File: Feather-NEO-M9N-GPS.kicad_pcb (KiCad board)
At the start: 2 copper layers, 50.8 x 22.9 mm, 60 parts, among them IC1 PRTR5V0U2F,115, J6 USB_B_Micro, U1 NEO-M9N, U2 AP2112K-3.3

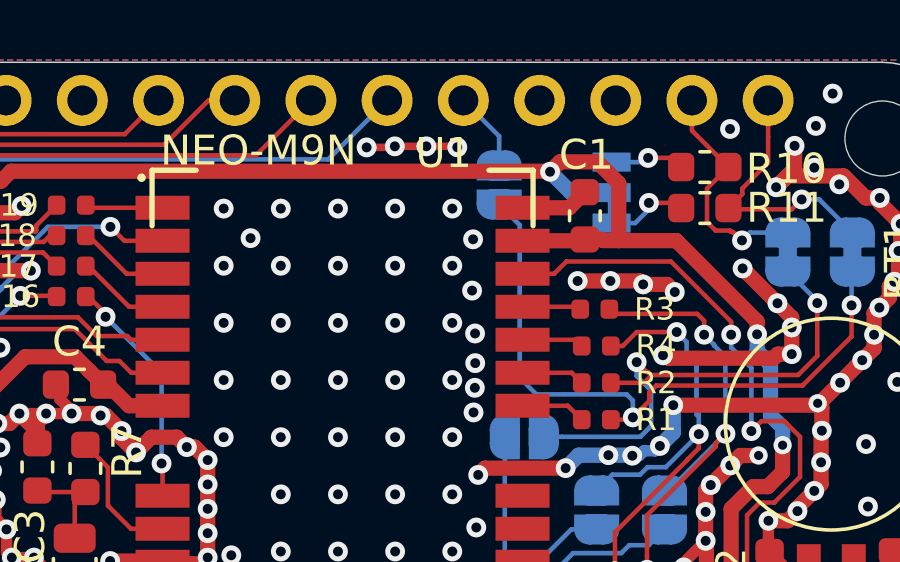
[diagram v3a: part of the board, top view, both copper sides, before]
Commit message: Added additional CS pin. Kept caps as is because of integration manual
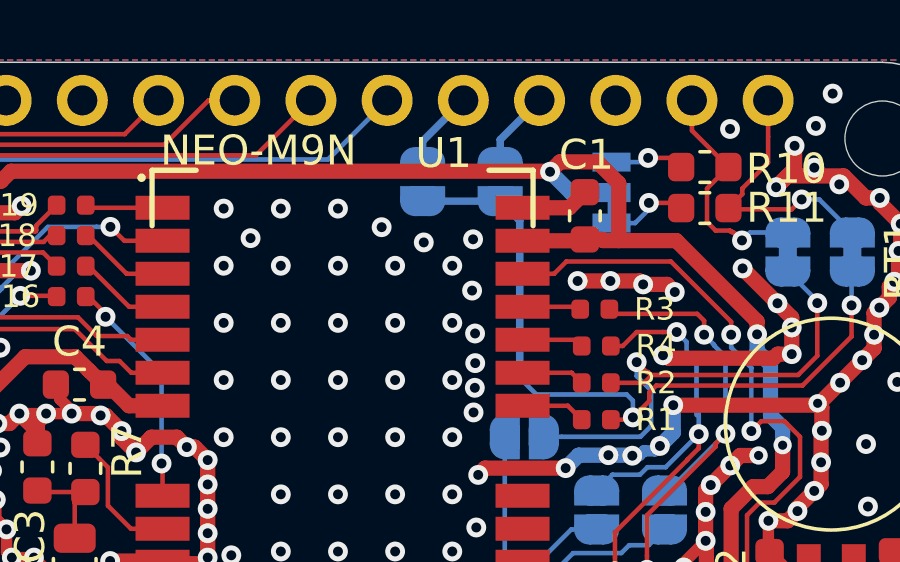
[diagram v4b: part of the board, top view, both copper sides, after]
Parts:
- added JP17: ~CS2, Jumper:SolderJumper-2_P1.3mm_Open_RoundedPad1.0x1.5mm, B.Cu at (164.2, 78.5)
- R13: value 1k -> 500
- moved JP16 2.55 mm to (161.6, 78.5)
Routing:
- net GND: track 237.1 -> 234.0 mm, vias 238 -> 234
- net Net-(JP16-Pad2): track 22.9 -> 25.5 mm
- net /6: track 0.00 -> 2.60 mm
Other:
- board text added: "6"
- board text added: "Rev2.4 ABW 3/6/20"
- board text removed: "Rev2.3 ABW 2/24/20"
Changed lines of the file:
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@@
   (general
     (thickness 1.6)
-    (drawings 21)
-    (tracks 1105)
+    (drawings 22)
+    (tracks 1099)
     (zones 0)
-    (modules 60)
+    (modules 61)
     (nets 73)
   )
@@
   )
   (setup
-    (last_trace_width 0.381)
+    (last_trace_width 0.1524)
     (user_trace_width 0.1524)
     (user_trace_width 0.1778)
@@
       (drillshape 0)
       (scaleselection 1)
-      (outputdirectory "Rev2.3/"))
+      (outputdirectory "Rev2.4/"))
   )
   (net 0 "")
@@
   )
   (module Jumper:SolderJumper-2_P1.3mm_Open_RoundedPad1.0x1.5mm (layer B.Cu)
+    (at 164.15766 78.47584 270)
+    (descr "SMD Solder Jumper, 1x1.5mm, rounded Pads, 0.3mm gap, open")
+    (tags "solder jumper open")
+    (attr virtual)
+    (fp_text reference JP17 (at 0 1.8 90) (layer B.Fab)
+      (effects (font (size 1 1) (thickness 0.15)) (justify mirror))
+    )
+    (fp_text value ~CS2 (at 0 -1.9 90) (layer B.Fab)
+      (effects (font (size 1 1) (thickness 0.15)) (justify mirror))
+    )
+    (fp_line (start 1.65 -1.25) (end -1.65 -1.25) (layer B.CrtYd) (width 0.05))
+    (fp_line (start 1.65 -1.25) (end 1.65 1.25) (layer B.CrtYd) (width 0.05))
+    (fp_line (start -1.65 1.25) (end -1.65 -1.25) (layer B.CrtYd) (width 0.05))
+    (fp_line (start -1.65 1.25) (end 1.65 1.25) (layer B.CrtYd) (width 0.05))
+    (fp_line (start -0.7 1) (end 0.7 1) (layer B.SilkS) (width 0.12))
+    (fp_line (start 1.4 0.3) (end 1.4 -0.3) (layer B.SilkS) (width 0.12))
+    (fp_line (start 0.7 -1) (end -0.7 -1) (layer B.SilkS) (width 0.12))
+    (fp_line (start -1.4 -0.3) (end -1.4 0.3) (layer B.SilkS) (width 0.12))
+    (fp_arc (start -0.7 0.3) (end -0.7 1) (angle 90) (layer B.SilkS) (width 0.12))
+    (fp_arc (start -0.7 -0.3) (end -1.4 -0.3) (angle 90) (layer B.SilkS) (width 0.12))
+    (fp_arc (start 0.7 -0.3) (end 0.7 -1) (angle 90) (layer B.SilkS) (width 0.12))
+    (fp_arc (start 0.7 0.3) (end 1.4 0.3) (angle 90) (layer B.SilkS) (width 0.12))
+    (pad 2 smd custom (at 0.65 0 270) (size 1 0.5) (layers B.Cu B.Mask)
+      (net 72 "Net-(JP16-Pad2)") (zone_connect 2)
+      (options (clearance outline) (anchor rect))
+      (primitives
+        (gr_circle (center 0 -0.25) (end 0.5 -0.25) (width 0))
+        (gr_circle (center 0 0.25) (end 0.5 0.25) (width 0))
+        (gr_poly (pts
+           (xy 0 0.75) (xy -0.5 0.75) (xy -0.5 -0.75) (xy 0 -0.75)) (width 0))
+      ))
+    (pad 1 smd custom (at -0.65 0 270) (size 1 0.5) (layers B.Cu B.Mask)
+      (net 7 /6) (zone_connect 2)
+      (options (clearance outline) (anchor rect))
+      (primitives
+        (gr_circle (center 0 -0.25) (end 0.5 -0.25) (width 0))
+        (gr_circle (center 0 0.25) (end 0.5 0.25) (width 0))
+        (gr_poly (pts
+           (xy 0 0.75) (xy 0.5 0.75) (xy 0.5 -0.75) (xy 0 -0.75)) (width 0))
+      ))
+  )
+  (module Jumper:SolderJumper-2_P1.3mm_Open_RoundedPad1.0x1.5mm (layer B.Cu)
     (at 164.9603 86.9823)
     (descr "SMD Solder Jumper, 1x1.5mm, rounded Pads, 0.3mm gap, open")
@@
   )
   (module Jumper:SolderJumper-2_P1.3mm_Open_RoundedPad1.0x1.5mm (layer B.Cu)
-    (at 164.1221 78.5876 270)
+    (at 161.57194 78.47584 270)
     (descr "SMD Solder Jumper, 1x1.5mm, rounded Pads, 0.3mm gap, open")
     (tags "solder jumper open")
@@
       (effects (font (size 1 1) (thickness 0.15)) (justify mirror))
     )
-    (fp_text value ~CS (at 0.0381 2.7305 180) (layer B.SilkS)
+    (fp_text value ~CS (at 2.81686 -1.01346 180) (layer B.SilkS)
       (effects (font (size 1 1) (thickness 0.15)) (justify mirror))
     )
@@
       (effects (font (size 1 1) (thickness 0.15)))
     )
-    (fp_text value 1k (at 0 1.43) (layer F.Fab)
+    (fp_text value 500 (at 0 1.43) (layer F.Fab)
       (effects (font (size 1 1) (thickness 0.15)))
     )
@@
     (pad 1 thru_hole circle (at 0 0) (size 3.8 3.8) (drill 2.2) (layers *.Cu *.Mask))
   )
-  (gr_text 9 (at 165.608 79.20228) (layer B.SilkS)
+  (gr_text 6 (at 165.7604 78.6638) (layer B.SilkS)
+    (effects (font (size 1 1) (thickness 0.15)) (justify mirror))
+  )
+  (gr_text 9 (at 159.7787 78.6638) (layer B.SilkS)
     (effects (font (size 1 1) (thickness 0.15)) (justify mirror))
   )
@@
     (arrow2b (pts (xy 128.6383 68.2371) (xy 129.764804 67.650679)))
   )
-  (gr_text "Rev2.3\nABW\n2/24/20" (at 139.60602 90.83294) (layer B.SilkS)
+  (gr_text "Rev2.4\nABW\n3/6/20" (at 139.60602 90.83294) (layer B.SilkS)
     (effects (font (size 1 1) (thickness 0.15)) (justify mirror))
   )
-  (gr_text "u-blox GPS\nNEO-M9N\nFeatherwing" (at 157.0101 82.1436) (layer B.SilkS)
+  (gr_text "u-blox GPS\nNEO-M9N\nFeatherwing" (at 154.9908 84.1248) (layer B.SilkS)
     (effects (font (size 1 1) (thickness 0.15)) (justify mirror))
   )
@@
   (segment (start 173.875701 79.400399) (end 171.808239 79.400399) (width 0.1524) (layer F.Cu) (net 5))
   (segment (start 174.2059 79.0702) (end 173.875701 79.400399) (width 0.1524) (layer F.Cu) (net 5))
-  (segment (start 164.1221 76.962) (end 162.9283 75.7682) (width 0.1524) (layer B.Cu) (net 8))
-  (segment (start 164.1221 77.9376) (end 164.1221 76.962) (width 0.1524) (layer B.Cu) (net 8))
+  (segment (start 164.15766 77.07884) (end 165.4683 75.7682) (width 0.25) (layer B.Cu) (net 7))
+  (segment (start 164.15766 77.82584) (end 164.15766 77.07884) (width 0.25) (layer B.Cu) (net 7))
+  (segment (start 161.57194 77.12456) (end 162.9283 75.7682) (width 0.25) (layer B.Cu) (net 8))
+  (segment (start 161.57194 77.82584) (end 161.57194 77.12456) (width 0.25) (layer B.Cu) (net 8))
   (segment (start 139.2809 81.7776) (end 139.2809 80.114682) (width 0.1524) (layer B.Cu) (net 9))
   (segment (start 138.4323 82.6262) (end 139.2809 81.7776) (width 0.1524) (layer B.Cu) (net 9))
@@
   (via (at 156.845 79.375) (size 0.6604) (drill 0.3302) (layers F.Cu B.Cu) (net 16))
   (via (at 158.75 79.375) (size 0.6604) (drill 0.3302) (layers F.Cu B.Cu) (net 16))
-  (via (at 160.655 79.375) (size 0.6604) (drill 0.3302) (layers F.Cu B.Cu) (net 16))
-  (via (at 162.56 79.375) (size 0.6604) (drill 0.3302) (layers F.Cu B.Cu) (net 16))
   (via (at 154.94 81.28) (size 0.6604) (drill 0.3302) (layers F.Cu B.Cu) (net 16))
   (via (at 156.845 81.28) (size 0.6604) (drill 0.3302) (layers F.Cu B.Cu) (net 16))
@@
   (via (at 155.83662 80.36052) (size 0.6604) (drill 0.3302) (layers F.Cu B.Cu) (net 16))
   (segment (start 134.81548 81.9658) (end 134.81548 81.85394) (width 0.381) (layer F.Cu) (net 16))
-  (via (at 159.70504 77.33538) (size 0.6604) (drill 0.3302) (layers F.Cu B.Cu) (net 16))
-  (via (at 160.64484 77.29982) (size 0.6604) (drill 0.3302) (layers F.Cu B.Cu) (net 16))
-  (via (at 161.6964 77.29982) (size 0.6604) (drill 0.3302) (layers F.Cu B.Cu) (net 16))
-  (via (at 162.72764 77.3303) (size 0.6604) (drill 0.3302) (layers F.Cu B.Cu) (net 16))
-  (segment (start 160.60928 77.33538) (end 160.64484 77.29982) (width 0.254) (layer F.Cu) (net 16))
-  (segment (start 159.70504 77.33538) (end 160.60928 77.33538) (width 0.254) (layer F.Cu) (net 16))
-  (segment (start 160.64484 77.29982) (end 161.6964 77.29982) (width 0.254) (layer F.Cu) (net 16))
-  (segment (start 162.69716 77.29982) (end 162.72764 77.3303) (width 0.254) (layer F.Cu) (net 16))
-  (segment (start 161.6964 77.29982) (end 162.69716 77.29982) (width 0.254) (layer F.Cu) (net 16))
   (segment (start 145.7579 79.9973) (end 146.2405 79.5147) (width 0.254) (layer B.Cu) (net 16))
   (segment (start 145.7579 81.4578) (end 145.7579 79.9973) (width 0.254) (layer B.Cu) (net 16))
@@
   (segment (start 133.80212 75.76312) (end 133.80212 76.55306) (width 0.381) (layer F.Cu) (net 16))
   (segment (start 134.12978 75.43546) (end 133.80212 75.76312) (width 0.381) (layer F.Cu) (net 16))
+  (via (at 160.20542 79.99476) (size 0.6604) (drill 0.3302) (layers F.Cu B.Cu) (net 16))
+  (via (at 161.61004 80.50276) (size 0.6604) (drill 0.3302) (layers F.Cu B.Cu) (net 16))
   (via (at 165.819651 78.147349) (size 0.6604) (drill 0.3302) (layers F.Cu B.Cu) (net 24))
   (segment (start 138.7298 94.2086) (end 143.0909 94.2086) (width 0.508) (layer F.Cu) (net 24))
@@
   (segment (start 165.363786 85.57011) (end 164.8079 85.014224) (width 0.1524) (layer B.Cu) (net 72))
   (segment (start 168.37411 85.57011) (end 165.363786 85.57011) (width 0.1524) (layer B.Cu) (net 72))
-  (segment (start 164.8079 79.9234) (end 164.1221 79.2376) (width 0.1524) (layer B.Cu) (net 72))
-  (segment (start 164.8079 85.014224) (end 164.8079 79.9234) (width 0.1524) (layer B.Cu) (net 72))
   (via (at 168.5798 86.3346) (size 0.6604) (drill 0.3302) (layers F.Cu B.Cu) (net 72))
   (segment (start 168.5798 85.7758) (end 168.5798 86.3346) (width 0.1524) (layer B.Cu) (net 72))
@@
   (segment (start 168.5036 86.4108) (end 168.5798 86.3346) (width 0.1524) (layer F.Cu) (net 72))
   (segment (start 167.8456 86.4108) (end 168.5036 86.4108) (width 0.1524) (layer F.Cu) (net 72))
+  (segment (start 161.57194 79.12584) (end 164.15766 79.12584) (width 0.25) (layer B.Cu) (net 72))
+  (segment (start 164.8079 79.77608) (end 164.15766 79.12584) (width 0.25) (layer B.Cu) (net 72))
+  (segment (start 164.8079 85.014224) (end 164.8079 79.77608) (width 0.25) (layer B.Cu) (net 72))
   (zone (net 16) (net_name GND) (layer F.Cu) (hatch edge 0.508)
     (connect_pads (clearance 0.508))

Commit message: Updates
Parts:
- moved D4 0.32 mm to (142.4, 88.9)
